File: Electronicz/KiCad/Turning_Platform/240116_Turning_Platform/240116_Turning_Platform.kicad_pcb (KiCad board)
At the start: 2 copper layers, 104.1 x 58.4 mm, 8 parts, among them J1 StepperMotor, J2 StepperDriverA, J3 StepperDriverB, J5 +12V, J6 GND, J7 Display, J8 RotaryEncoder

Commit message: Update Turning Platform PCB
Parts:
- added REF**: MountingHole_3.5mm, MountingHole:MountingHole_3.5mm, F.Cu at (193.0, 58.4)
- added REF**: MountingHole_3.5mm, MountingHole:MountingHole_3.5mm, F.Cu at (96.5, 58.4)
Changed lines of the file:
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@@
     )
+  )
+  (footprint "MountingHole:MountingHole_3.5mm" (layer "F.Cu")
+    (at 193.04 58.42)
+    (descr "Mounting Hole 3.5mm, no annular")
+    (tags "mounting hole 3.5mm no annular")
+    (attr exclude_from_pos_files exclude_from_bom)
+    (fp_text reference "REF**" (at 0 -4.5) (layer "F.SilkS")
+        (effects (font (size 1 1) (thickness 0.15)))
+    )
+    (fp_text value "MountingHole_3.5mm" (at 0 4.5) (layer "F.Fab")
+        (effects (font (size 1 1) (thickness 0.15)))
+    )
+    (fp_text user "${REFERENCE}" (at 0 0) (layer "F.Fab")
+        (effects (font (size 1 1) (thickness 0.15)))
+    )
+    (fp_circle (center 0 0) (end 3.5 0)
+      (stroke (width 0.15) (type solid)) (fill none) (layer "Cmts.User"))
+    (fp_circle (center 0 0) (end 3.75 0)
+      (stroke (width 0.05) (type solid)) (fill none) (layer "F.CrtYd"))
+    (pad "" np_thru_hole circle (at 0 0) (size 3.5 3.5) (drill 3.5) (layers "*.Cu" "*.Mask"))
   )
   (footprint "Connector_PinHeader_2.54mm:PinHeader_1x01_P2.54mm_Vertical" (layer "F.Cu")
@@
     )
   )
+  (footprint "MountingHole:MountingHole_3.5mm" (layer "F.Cu")
+    (at 96.52 58.42)
+    (descr "Mounting Hole 3.5mm, no annular")
+    (tags "mounting hole 3.5mm no annular")
+    (attr exclude_from_pos_files exclude_from_bom)
+    (fp_text reference "REF**" (at 0 -4.5) (layer "F.SilkS")
+        (effects (font (size 1 1) (thickness 0.15)))
+    )
+    (fp_text value "MountingHole_3.5mm" (at 0 4.5) (layer "F.Fab")
+        (effects (font (size 1 1) (thickness 0.15)))
+    )
+    (fp_text user "${REFERENCE}" (at 0 0) (layer "F.Fab")
+        (effects (font (size 1 1) (thickness 0.15)))
+    )
+    (fp_circle (center 0 0) (end 3.5 0)
+      (stroke (width 0.15) (type solid)) (fill none) (layer "Cmts.User"))
+    (fp_circle (center 0 0) (end 3.75 0)
+      (stroke (width 0.05) (type solid)) (fill none) (layer "F.CrtYd"))
+    (pad "" np_thru_hole circle (at 0 0) (size 3.5 3.5) (drill 3.5) (layers "*.Cu" "*.Mask"))
+  )
   (footprint "Connector_PinHeader_2.54mm:PinHeader_1x01_P2.54mm_Vertical" (layer "F.Cu")

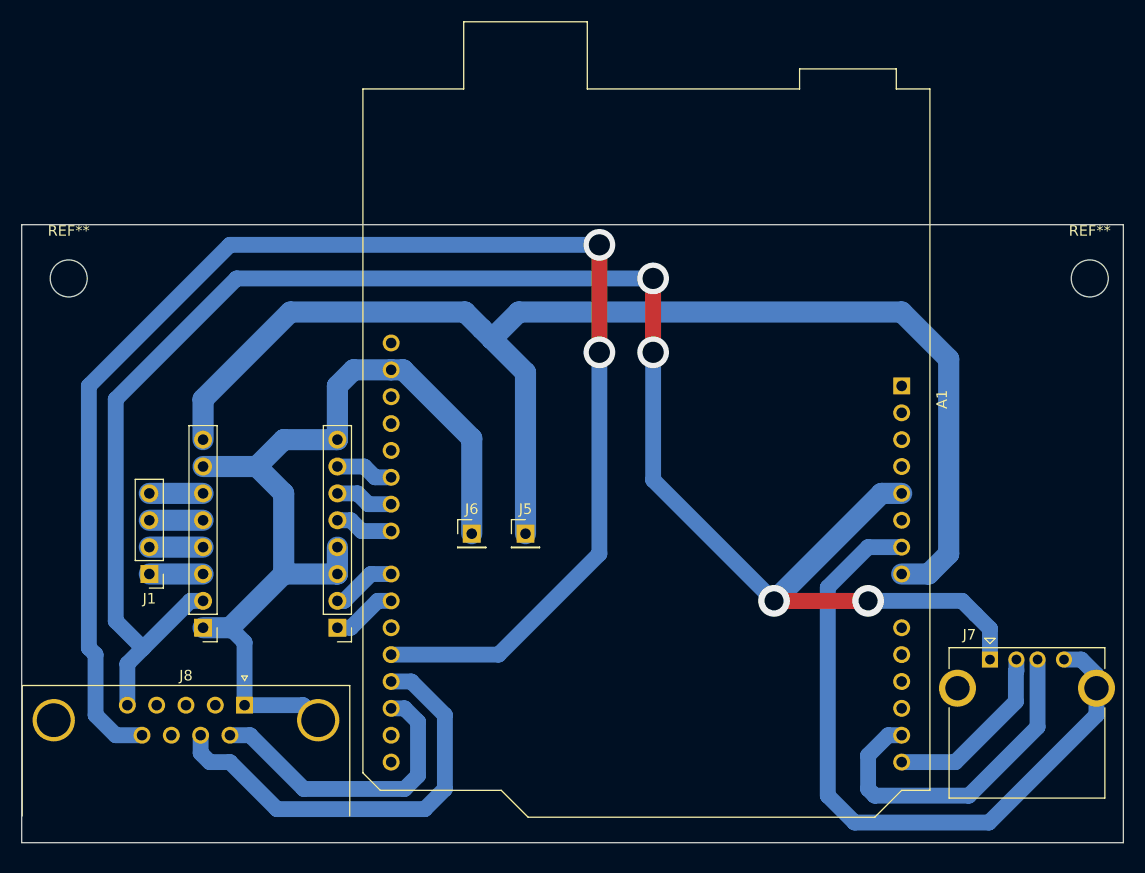
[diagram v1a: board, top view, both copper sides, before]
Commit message: Update Turning Platform PCB
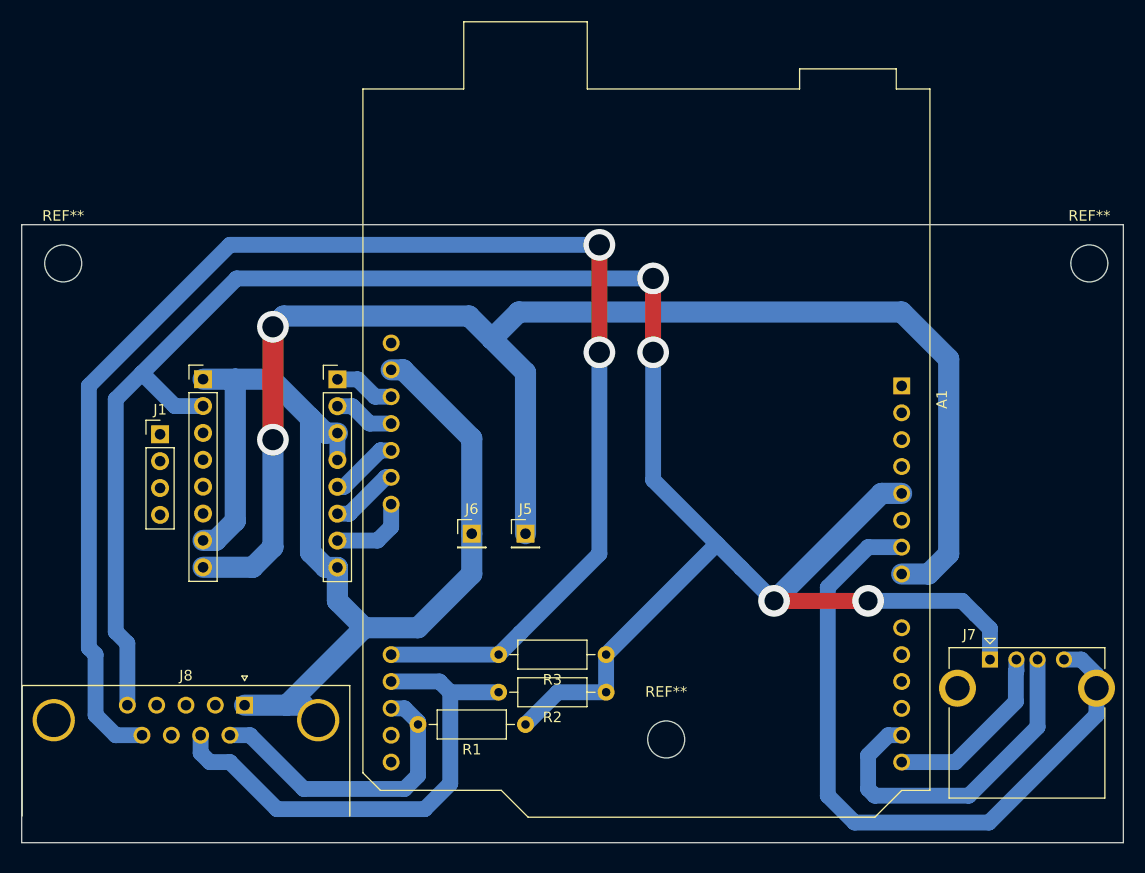
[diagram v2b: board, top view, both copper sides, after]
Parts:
- added R1: 100, Resistor_THT:R_Axial_DIN0207_L6.3mm_D2.5mm_P10.16mm_Horizontal, F.Cu at (139.7, 100.6)
- added R2: 100, Resistor_THT:R_Axial_DIN0207_L6.3mm_D2.5mm_P10.16mm_Horizontal, F.Cu at (147.3, 97.5)
- added R3: 100, Resistor_THT:R_Axial_DIN0207_L6.3mm_D2.5mm_P10.16mm_Horizontal, F.Cu at (147.3, 94.0)
- added REF**: MountingHole_3.5mm, MountingHole:MountingHole_3.5mm, F.Cu at (153.0, 102.0)
- moved J2 23.5 mm to (109.2, 67.9), turned to 0 degrees
- moved J3 23.5 mm to (121.9, 68.0), turned to 0 degrees
- moved J1 13.2 mm to (105.2, 73.2), turned to 0 degrees
- moved REF** 1.51 mm to (96.0, 57.0)
- moved REF** 1.42 mm to (193.0, 57.0)
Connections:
- A1 pad 26: unconnected-(A1-D11-Pad26) -> Net-(A1-D11)
- A1 pad 27: unconnected-(A1-D12-Pad27) -> Net-(A1-D12)
- A1 pad 28: unconnected-(A1-D13-Pad28) -> Net-(A1-D13)
- J3 pad 1: Net-(A1-D6) -> Net-(A1-D13)
- J3 pad 2: Net-(A1-D7) -> Net-(A1-D12)
- J3 pad 5: Net-(A1-D8) -> Net-(A1-D11)
- J3 pad 6: Net-(A1-D9) -> Net-(A1-D10)
- J3 pad 7: Net-(A1-D10) -> Net-(A1-D9)
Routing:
- net Net-(A1-+5V): track 170.2 -> 195.8 mm
- net Net-(J2-Pin_1): track 87.8 -> 111.9 mm
- net Net-(A1-VIN): track 125.0 -> 139.7 mm, vias 0 -> 2
- net Net-(A1-D3): track 41.1 -> 47.7 mm
- net Net-(A1-D11): track 0.00 -> 6.51 mm
- net Net-(A1-D7): track 6.13 -> 0.00 mm
- net Net-(A1-D6): track 6.13 -> 0.00 mm
- net Net-(A1-D13): track 0.00 -> 5.76 mm
- net Net-(A1-D12): track 0.00 -> 5.76 mm
- net Net-(A1-D8): track 5.50 -> 0.00 mm
- net Net-(J1-Pin_4): track 5.08 -> 0.00 mm
- net Net-(J1-Pin_3): track 5.08 -> 0.00 mm
- net Net-(J1-Pin_2): track 5.08 -> 0.00 mm
- net Net-(J1-Pin_1): track 5.08 -> 0.00 mm
- net Net-(A1-D9): track 5.50 -> 7.77 mm
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
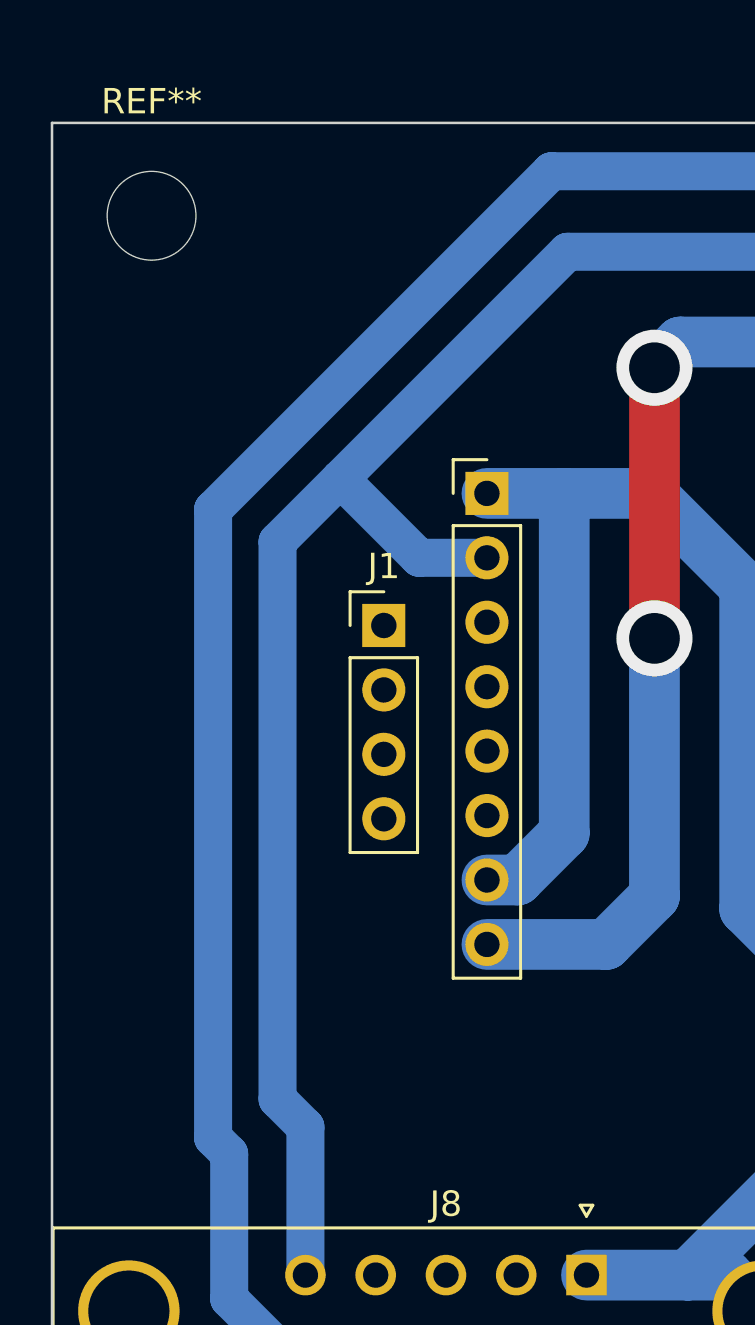
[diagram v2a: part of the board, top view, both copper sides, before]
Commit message: Update Stepper Motor Connections
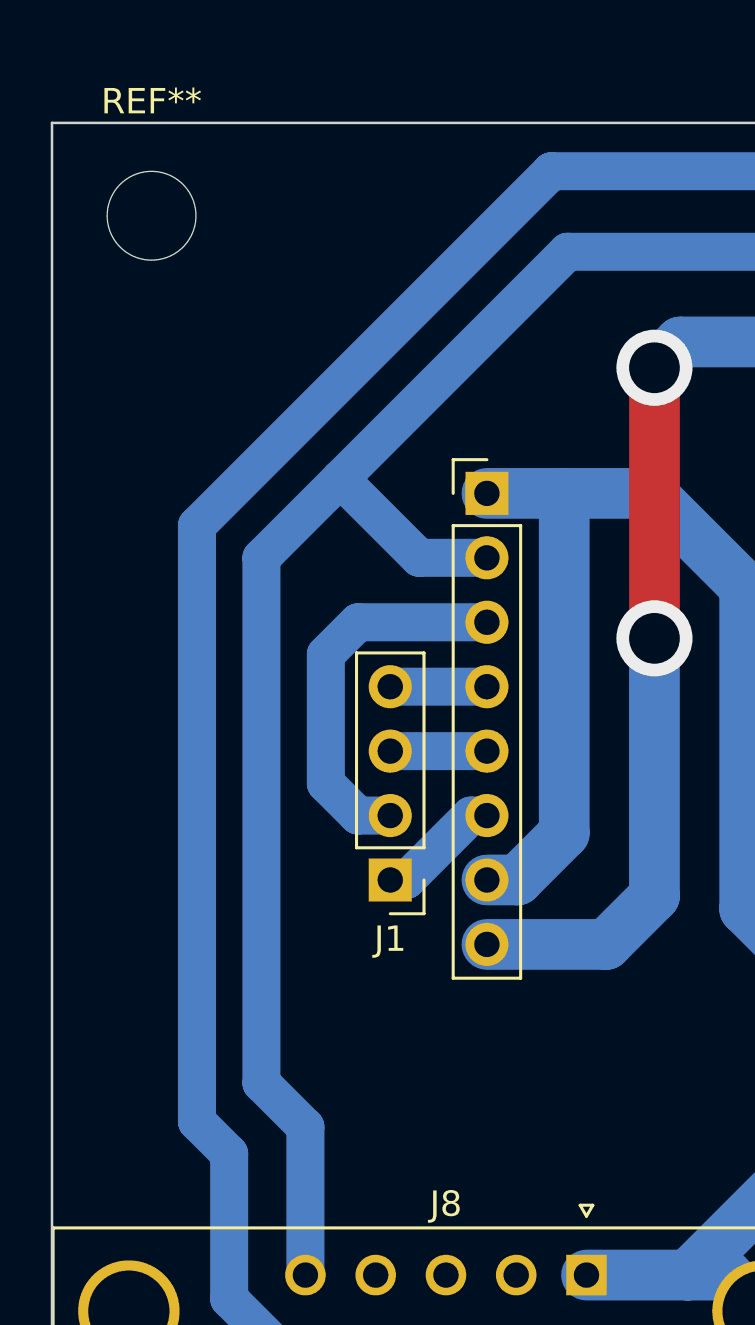
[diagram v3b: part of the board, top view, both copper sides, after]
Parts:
- moved J1 10.0 mm to (105.4, 83.2), turned to 180 degrees
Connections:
- J2 pad 3: Net-(J1-Pin_1) -> Net-(J1-Pin_2)
- J2 pad 4: Net-(J1-Pin_2) -> Net-(J1-Pin_4)
- J2 pad 6: Net-(J1-Pin_4) -> Net-(J1-Pin_1)
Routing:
- net Net-(J1-Pin_2): track 0.00 -> 15.0 mm
- net Net-(J1-Pin_1): track 0.00 -> 4.86 mm
- net Net-(J1-Pin_4): track 0.00 -> 3.81 mm
- net Net-(J1-Pin_3): track 0.00 -> 3.81 mm
- net Net-(A1-D4): track 143.8 -> 144.3 mm
- net Net-(A1-+5V): track 195.8 -> 196.3 mm
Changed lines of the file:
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@@
   )
   (footprint "Connector_PinHeader_2.54mm:PinHeader_1x04_P2.54mm_Vertical" (layer "F.Cu")
-    (at 105.156 73.152)
+    (at 105.41 83.185 180)
     (descr "Through hole straight pin header, 1x04, 2.54mm pitch, single row")
     (tags "Through hole pin header THT 1x04 2.54mm single row")
@@
     (fp_line (start 1.27 8.89) (end -1.27 8.89)
       (stroke (width 0.1) (type solid)) (layer "F.Fab"))
-    (pad "1" thru_hole rect (at 0 0) (size 1.7 1.7) (drill 1) (layers "*.Cu" "*.Mask")
+    (pad "1" thru_hole rect (at 0 0 180) (size 1.7 1.7) (drill 1) (layers "*.Cu" "*.Mask")
       (net 27 "Net-(J1-Pin_1)") (pinfunction "Pin_1") (pintype "passive"))
-    (pad "2" thru_hole oval (at 0 2.54) (size 1.7 1.7) (drill 1) (layers "*.Cu" "*.Mask")
+    (pad "2" thru_hole oval (at 0 2.54 180) (size 1.7 1.7) (drill 1) (layers "*.Cu" "*.Mask")
       (net 28 "Net-(J1-Pin_2)") (pinfunction "Pin_2") (pintype "passive"))
-    (pad "3" thru_hole oval (at 0 5.08) (size 1.7 1.7) (drill 1) (layers "*.Cu" "*.Mask")
+    (pad "3" thru_hole oval (at 0 5.08 180) (size 1.7 1.7) (drill 1) (layers "*.Cu" "*.Mask")
       (net 29 "Net-(J1-Pin_3)") (pinfunction "Pin_3") (pintype "passive"))
-    (pad "4" thru_hole oval (at 0 7.62) (size 1.7 1.7) (drill 1) (layers "*.Cu" "*.Mask")
+    (pad "4" thru_hole oval (at 0 7.62 180) (size 1.7 1.7) (drill 1) (layers "*.Cu" "*.Mask")
       (net 30 "Net-(J1-Pin_4)") (pinfunction "Pin_4") (pintype "passive"))
     (model "${KICAD6_3DMODEL_DIR}/Connector_PinHeader_2.54mm.3dshapes/PinHeader_1x04_P2.54mm_Vertical.wrl"
@@
       (net 5 "Net-(A1-+5V)") (pinfunction "Pin_2") (pintype "passive"))
     (pad "3" thru_hole oval (at 0 5.08) (size 1.7 1.7) (drill 1) (layers "*.Cu" "*.Mask")
-      (net 27 "Net-(J1-Pin_1)") (pinfunction "Pin_3") (pintype "passive"))
+      (net 28 "Net-(J1-Pin_2)") (pinfunction "Pin_3") (pintype "passive"))
     (pad "4" thru_hole oval (at 0 7.62) (size 1.7 1.7) (drill 1) (layers "*.Cu" "*.Mask")
-      (net 28 "Net-(J1-Pin_2)") (pinfunction "Pin_4") (pintype "passive"))
+      (net 30 "Net-(J1-Pin_4)") (pinfunction "Pin_4") (pintype "passive"))
     (pad "5" thru_hole oval (at 0 10.16) (size 1.7 1.7) (drill 1) (layers "*.Cu" "*.Mask")
       (net 29 "Net-(J1-Pin_3)") (pinfunction "Pin_5") (pintype "passive"))
     (pad "6" thru_hole oval (at 0 12.7) (size 1.7 1.7) (drill 1) (layers "*.Cu" "*.Mask")
-      (net 30 "Net-(J1-Pin_4)") (pinfunction "Pin_6") (pintype "passive"))
+      (net 27 "Net-(J1-Pin_1)") (pinfunction "Pin_6") (pintype "passive"))
     (pad "7" thru_hole oval (at 0 15.24) (size 1.7 1.7) (drill 1) (layers "*.Cu" "*.Mask")
       (net 25 "Net-(J2-Pin_1)") (pinfunction "Pin_7") (pintype "passive"))
@@
   (via (at 151.765 65.405) (size 3) (drill 2) (layers "F.Cu" "B.Cu") (net 5))
   (via (at 151.765 58.42) (size 3) (drill 2) (layers "F.Cu" "B.Cu") (net 5))
-  (segment (start 102.065 92.921) (end 100.965 91.821) (width 1.5) (layer "B.Cu") (net 5))
-  (segment (start 100.965 69.85) (end 103.4415 67.3735) (width 1.5) (layer "B.Cu") (net 5))
+  (segment (start 100.33 70.485) (end 103.4415 67.3735) (width 1.5) (layer "B.Cu") (net 5))
+  (segment (start 100.33 91.186) (end 100.33 70.485) (width 1.5) (layer "B.Cu") (net 5))
   (segment (start 160.0835 85.7885) (end 163.195 88.9) (width 1.5) (layer "B.Cu") (net 5))
   (segment (start 183.605 94.445) (end 183.605 91.53) (width 1.5) (layer "B.Cu") (net 5))
   (segment (start 173.355 78.74) (end 175.26 78.74) (width 2) (layer "B.Cu") (net 5))
+  (segment (start 102.065 98.76) (end 102.065 92.921) (width 1.5) (layer "B.Cu") (net 5))
   (segment (start 151.765 64.77) (end 151.765 77.47) (width 1.5) (layer "B.Cu") (net 5))
   (segment (start 157.7975 83.5025) (end 160.0835 85.7885) (width 1.5) (layer "B.Cu") (net 5))
@@
   (segment (start 163.195 88.9) (end 173.355 78.74) (width 2) (layer "B.Cu") (net 5))
   (segment (start 109.22 70.485) (end 106.553 70.485) (width 1.5) (layer "B.Cu") (net 5))
-  (segment (start 100.965 91.821) (end 100.965 69.85) (width 1.5) (layer "B.Cu") (net 5))
   (segment (start 142.748 97.536) (end 147.32 97.536) (width 1.5) (layer "B.Cu") (net 5))
   (segment (start 103.4415 67.3735) (end 112.395 58.42) (width 1.5) (layer "B.Cu") (net 5))
   (segment (start 182.245 90.17) (end 180.975 88.9) (width 1.5) (layer "B.Cu") (net 5))
+  (segment (start 102.065 92.921) (end 100.33 91.186) (width 1.5) (layer "B.Cu") (net 5))
   (segment (start 151.765 77.47) (end 157.7975 83.5025) (width 1.5) (layer "B.Cu") (net 5))
-  (segment (start 102.065 98.76) (end 102.065 92.921) (width 1.5) (layer "B.Cu") (net 5))
   (segment (start 112.395 58.42) (end 151.765 58.42) (width 1.5) (layer "B.Cu") (net 5))
   (segment (start 147.32 93.98) (end 157.7975 83.5025) (width 1.5) (layer "B.Cu") (net 5))
@@
   (via (at 146.685 65.405) (size 3) (drill 2) (layers "F.Cu" "B.Cu") (net 19))
   (via (at 146.685 55.245) (size 3) (drill 2) (layers "F.Cu" "B.Cu") (net 19))
-  (segment (start 98.425 93.345) (end 98.425 68.58) (width 1.5) (layer "B.Cu") (net 19))
+  (segment (start 99.06 99.695) (end 99.06 93.98) (width 1.5) (layer "B.Cu") (net 19))
+  (segment (start 99.06 93.98) (end 97.79 92.71) (width 1.5) (layer "B.Cu") (net 19))
+  (segment (start 97.79 69.215) (end 111.76 55.245) (width 1.5) (layer "B.Cu") (net 19))
+  (segment (start 146.685 64.77) (end 146.685 84.455) (width 1.5) (layer "B.Cu") (net 19))
+  (segment (start 97.79 92.71) (end 97.79 69.215) (width 1.5) (layer "B.Cu") (net 19))
+  (segment (start 111.76 55.245) (end 146.685 55.245) (width 1.5) (layer "B.Cu") (net 19))
+  (segment (start 139.192 91.948) (end 137.16 93.98) (width 1.5) (layer "B.Cu") (net 19))
+  (segment (start 137.16 93.98) (end 127 93.98) (width 1.5) (layer "B.Cu") (net 19))
+  (segment (start 146.685 84.455) (end 139.192 91.948) (width 1.5) (layer "B.Cu") (net 19))
   (segment (start 103.45 101.6) (end 100.965 101.6) (width 1.5) (layer "B.Cu") (net 19))
   (segment (start 100.965 101.6) (end 99.06 99.695) (width 1.5) (layer "B.Cu") (net 19))
-  (segment (start 146.685 64.77) (end 146.685 84.455) (width 1.5) (layer "B.Cu") (net 19))
-  (segment (start 98.425 68.58) (end 111.76 55.245) (width 1.5) (layer "B.Cu") (net 19))
-  (segment (start 139.192 91.948) (end 137.16 93.98) (width 1.5) (layer "B.Cu") (net 19))
-  (segment (start 137.16 93.98) (end 127 93.98) (width 1.5) (layer "B.Cu") (net 19))
-  (segment (start 111.76 55.245) (end 146.685 55.245) (width 1.5) (layer "B.Cu") (net 19))
-  (segment (start 146.685 84.455) (end 139.192 91.948) (width 1.5) (layer "B.Cu") (net 19))
-  (segment (start 99.06 99.695) (end 99.06 93.98) (width 1.5) (layer "B.Cu") (net 19))
-  (segment (start 99.06 93.98) (end 98.425 93.345) (width 1.5) (layer "B.Cu") (net 19))
   (segment (start 125.715 83.2) (end 127 81.915) (width 1.5) (layer "B.Cu") (net 20))
   (segment (start 127 81.915) (end 127 79.76) (width 1.5) (layer "B.Cu") (net 20))
@@
   (segment (start 121.92 85.74) (end 120.792 85.74) (width 2) (layer "B.Cu") (net 25))
   (segment (start 129.54 91.44) (end 124.46 91.44) (width 2) (layer "B.Cu") (net 25))
+  (segment (start 106.045 83.185) (end 108.585 80.645) (width 1.5) (layer "B.Cu") (net 27))
+  (segment (start 108.585 80.645) (end 109.22 80.645) (width 1.5) (layer "B.Cu") (net 27))
+  (segment (start 105.41 83.185) (end 106.045 83.185) (width 1.5) (layer "B.Cu") (net 27))
+  (segment (start 105.41 80.645) (end 104.14 80.645) (width 1.5) (layer "B.Cu") (net 28))
+  (segment (start 104.14 80.645) (end 102.87 79.375) (width 1.5) (layer "B.Cu") (net 28))
+  (segment (start 102.87 79.375) (end 102.87 74.295) (width 1.5) (layer "B.Cu") (net 28))
+  (segment (start 102.87 74.295) (end 104.14 73.025) (width 1.5) (layer "B.Cu") (net 28))
+  (segment (start 104.14 73.025) (end 109.22 73.025) (width 1.5) (layer "B.Cu") (net 28))
+  (segment (start 105.41 78.105) (end 109.22 78.105) (width 1.5) (layer "B.Cu") (net 29))
+  (segment (start 109.22 75.565) (end 105.41 75.565) (width 1.5) (layer "B.Cu") (net 30))
 )
